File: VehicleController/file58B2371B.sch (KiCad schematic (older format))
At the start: 8 parts, among them Q3 Q_NMOS_GDS, U12 FGMMOPA6H, U13 U.FL_Antenna

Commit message: Re-do MX120, GDS->GSD, Associations.
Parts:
- removed Q3: Q_NMOS_GDS, TO_SOT_Packages_SMD:SOT-23_Handsoldering, symbol Q_NMOS_GDS
- added Q3: Q_NMOS_GSD, TO_SOT_Packages_SMD:SOT-23_Handsoldering, symbol Q_NMOS_GSD
- U12: footprint UNCAMotorsports:GPS_16x16 -> UNCA Motorsports:GPS_16x16
- U13: footprint UNCAMotorsports:U.FL-CON -> UNCA Motorsports:U.FL-CON
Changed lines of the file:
@@
 F 0 "U12" H 7000 3837 60  0000 C CNN
 F 1 "FGMMOPA6H" H 7000 3731 60  0000 C CNN
-F 2 "UNCAMotorsports:GPS_16x16" H 6950 3400 60  0001 C CNN
+F 2 "UNCA Motorsports:GPS_16x16" H 6950 3400 60  0001 C CNN
 F 3 "" H 6950 3400 60  0000 C CNN
 	1    6950 3150
@@
 $EndComp
 $Comp
-L GND #PWR53
+L GND #PWR051
 U 1 1 58B24137
 P 5450 3800
-F 0 "#PWR53" H 5450 3550 50  0001 C CNN
+F 0 "#PWR051" H 5450 3550 50  0001 C CNN
 F 1 "GND" H 5455 3627 50  0000 C CNN
 F 2 "" H 5450 3800 50  0000 C CNN
@@
 F 0 "U13" H 7700 3500 60  0000 C CNN
 F 1 "U.FL_Antenna" H 8150 3800 60  0001 C CNN
-F 2 "UNCAMotorsports:U.FL-CON" H 7850 3650 60  0001 C CNN
+F 2 "UNCA Motorsports:U.FL-CON" H 7850 3650 60  0001 C CNN
 F 3 "" H 7850 3650 60  0000 C CNN
 	1    7850 3650
@@
 $EndComp
 $Comp
-L GND #PWR54
+L GND #PWR052
 U 1 1 58B24148
 P 8100 4050
-F 0 "#PWR54" H 8100 3800 50  0001 C CNN
+F 0 "#PWR052" H 8100 3800 50  0001 C CNN
 F 1 "GND" H 8105 3877 50  0000 C CNN
 F 2 "" H 8100 4050 50  0000 C CNN
@@
 VBACKUP
 $Comp
-L +3.3V #PWR52
+L +3.3V #PWR053
 U 1 1 58B276E4
 P 5450 2300
-F 0 "#PWR52" H 5450 2150 50  0001 C CNN
+F 0 "#PWR053" H 5450 2150 50  0001 C CNN
 F 1 "+3.3V" H 5465 2473 50  0000 C CNN
 F 2 "" H 5450 2300 50  0000 C CNN
@@
 $EndComp
 $Comp
-L GND #PWR51
+L GND #PWR054
 U 1 1 58B23C84
 P 3700 3600
-F 0 "#PWR51" H 3700 3350 50  0001 C CNN
+F 0 "#PWR054" H 3700 3350 50  0001 C CNN
 F 1 "GND" H 3705 3427 50  0000 C CNN
 F 2 "" H 3700 3600 50  0000 C CNN
@@
 $EndComp
 $Comp
-L Q_NMOS_GDS Q3
-U 1 1 58B23C7C
-P 3800 3300
-F 0 "Q3" H 4006 3346 50  0000 L CNN
-F 1 "Q_NMOS_GDS" H 4006 3255 50  0000 L CNN
-F 2 "TO_SOT_Packages_SMD:SOT-23_Handsoldering" H 4000 3400 50  0001 C CNN
-F 3 "" H 3800 3300 50  0000 C CNN
-	1    3800 3300
-	-1   0    0    -1
-$EndComp
-$Comp
-L +3.3V #PWR50
+L +3.3V #PWR055
 U 1 1 58B23C75
 P 3700 2400
-F 0 "#PWR50" H 3700 2250 50  0001 C CNN
+F 0 "#PWR055" H 3700 2250 50  0001 C CNN
 F 1 "+3.3V" H 3715 2573 50  0000 C CNN
 F 2 "" H 3700 2400 50  0000 C CNN
@@
 	0    -1   -1   0
 $EndComp
+$Comp
+L Q_NMOS_GSD Q3
+U 1 1 591B9790
+P 3800 3300
+F 0 "Q3" H 4000 3350 50  0000 L CNN
+F 1 "Q_NMOS_GSD" H 4000 3250 50  0000 L CNN
+F 2 "TO_SOT_Packages_SMD:SOT-23_Handsoldering" H 4000 3400 50  0001 C CNN
+F 3 "" H 3800 3300 50  0001 C CNN
+	1    3800 3300
+	-1   0    0    -1
+$EndComp
 $EndSCHEMATC

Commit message: Library Fixes
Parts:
- U12: footprint UNCA Motorsports:GPS_16x16 -> UNCAMotorsports:GPS_16x16
- U13: footprint UNCA Motorsports:U.FL-CON -> UNCAMotorsports:U.FL-CON
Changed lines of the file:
@@
 F 0 "U12" H 7000 3837 60  0000 C CNN
 F 1 "FGMMOPA6H" H 7000 3731 60  0000 C CNN
-F 2 "UNCA Motorsports:GPS_16x16" H 6950 3400 60  0001 C CNN
+F 2 "UNCAMotorsports:GPS_16x16" H 6950 3400 60  0001 C CNN
 F 3 "" H 6950 3400 60  0000 C CNN
 	1    6950 3150
@@
 F 0 "U13" H 7700 3500 60  0000 C CNN
 F 1 "U.FL_Antenna" H 8150 3800 60  0001 C CNN
-F 2 "UNCA Motorsports:U.FL-CON" H 7850 3650 60  0001 C CNN
+F 2 "UNCAMotorsports:U.FL-CON" H 7850 3650 60  0001 C CNN
 F 3 "" H 7850 3650 60  0000 C CNN
 	1    7850 3650

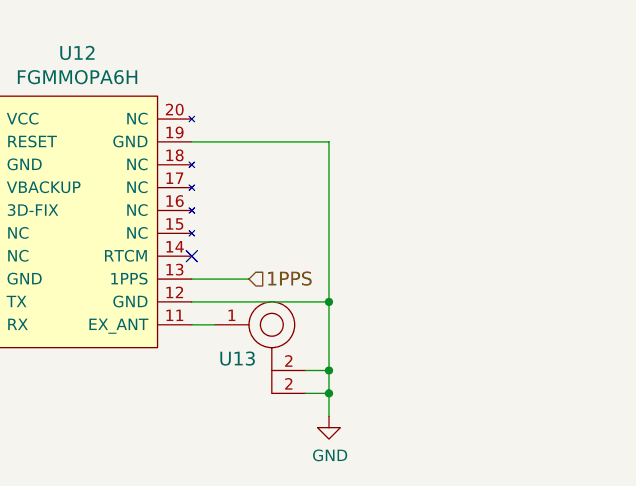
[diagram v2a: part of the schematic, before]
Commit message: Small schematic fixes, start layout
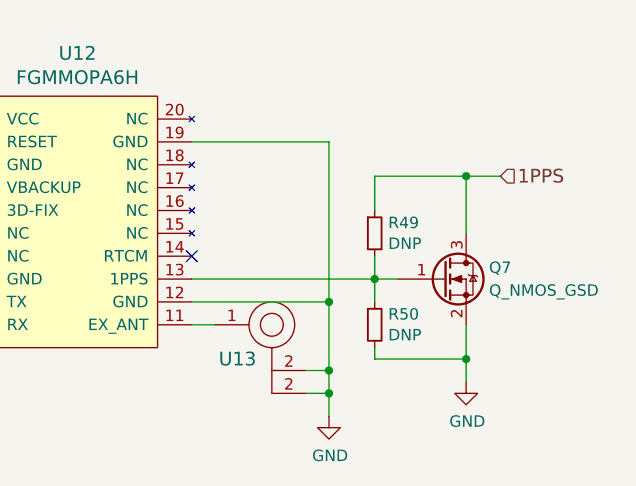
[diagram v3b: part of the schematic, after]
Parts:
- added Q7: Q_NMOS_GSD, TO_SOT_Packages_SMD:SOT-23_Handsoldering, symbol Q_NMOS_GSD
- added R49, R50: DNP, Resistors_SMD:R_0805_HandSoldering, symbol R_Small
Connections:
- net 1PPS: now also Q7.3 (D), R49.1; no longer U12.13 (1PPS)
- net GND: now also Q7.2 (S), R50.2
- new net: Q7.1 (G), R49.2, R50.1, U12.13 (1PPS)
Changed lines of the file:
@@
 LIBS:VehicleController-rescue
 LIBS:UNCAMotorsports
-LIBS:power
-LIBS:device
-LIBS:transistors
-LIBS:conn
-LIBS:linear
-LIBS:regul
-LIBS:74xx
-LIBS:cmos4000
-LIBS:adc-dac
-LIBS:memory
-LIBS:xilinx
-LIBS:microcontrollers
-LIBS:dsp
-LIBS:microchip
-LIBS:analog_switches
-LIBS:motorola
-LIBS:texas
-LIBS:intel
-LIBS:audio
-LIBS:interface
-LIBS:digital-audio
-LIBS:philips
-LIBS:display
-LIBS:cypress
-LIBS:siliconi
-LIBS:opto
-LIBS:atmel
-LIBS:contrib
-LIBS:valves
 LIBS:Common-Parts-Library-CPL
 LIBS:relays
 LIBS:SystemBlocks
-LIBS:dc-dc
-LIBS:Power_Management
-LIBS:switches
 LIBS:VehicleController-cache
-EELAYER 25 0
+EELAYER 26 0
 EELAYER END
 $Descr A4 11693 8268
@@
 Text HLabel 4250 3300 2    60   Input ~ 0
 3D-FIX
-Text HLabel 7750 3450 2    60   Input ~ 0
+Text HLabel 8850 3000 2    60   Input ~ 0
 1PPS
 Text HLabel 6050 2850 0    60   Input ~ 0
@@
 Connection ~ 8100 3850
 Wire Wire Line
-	7500 3450 7750 3450
+	7500 3450 8400 3450
 Wire Wire Line
 	7500 3550 8100 3550
@@
 	-1   0    0    -1
 $EndComp
+$Comp
+L Q_NMOS_GSD Q7
+U 1 1 591A0E4B
+P 8600 3450
+F 0 "Q7" H 8800 3500 50  0000 L CNN
+F 1 "Q_NMOS_GSD" H 8800 3400 50  0000 L CNN
+F 2 "TO_SOT_Packages_SMD:SOT-23_Handsoldering" H 8800 3550 50  0001 C CNN
+F 3 "" H 8600 3450 50  0001 C CNN
+	1    8600 3450
+	1    0    0    -1
+$EndComp
+Wire Wire Line
+	8300 3000 8850 3000
+Wire Wire Line
+	8700 3000 8700 3250
+$Comp
+L R_Small R49
+U 1 1 591A10E5
+P 8300 3250
+F 0 "R49" H 8359 3296 50  0000 L CNN
+F 1 "DNP" H 8359 3205 50  0000 L CNN
+F 2 "Resistors_SMD:R_0805_HandSoldering" H 8300 3250 50  0001 C CNN
+F 3 "" H 8300 3250 50  0001 C CNN
+	1    8300 3250
+	1    0    0    -1
+$EndComp
+Wire Wire Line
+	8300 3150 8300 3000
+Connection ~ 8700 3000
+Wire Wire Line
+	8300 3350 8300 3550
+Connection ~ 8300 3450
+$Comp
+L R_Small R50
+U 1 1 591A11A1
+P 8300 3650
+F 0 "R50" H 8359 3696 50  0000 L CNN
+F 1 "DNP" H 8359 3605 50  0000 L CNN
+F 2 "Resistors_SMD:R_0805_HandSoldering" H 8300 3650 50  0001 C CNN
+F 3 "" H 8300 3650 50  0001 C CNN
+	1    8300 3650
+	1    0    0    -1
+$EndComp
+Wire Wire Line
+	8300 3750 8300 3800
+Wire Wire Line
+	8300 3800 8700 3800
+Wire Wire Line
+	8700 3650 8700 3900
+$Comp
+L GND #PWR056
+U 1 1 591A124C
+P 8700 3900
+F 0 "#PWR056" H 8700 3650 50  0001 C CNN
+F 1 "GND" H 8705 3727 50  0000 C CNN
+F 2 "" H 8700 3900 50  0000 C CNN
+F 3 "" H 8700 3900 50  0000 C CNN
+	1    8700 3900
+	1    0    0    -1
+$EndComp
+Connection ~ 8700 3800
 $EndSCHEMATC
